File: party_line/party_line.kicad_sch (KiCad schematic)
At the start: 39 parts, among them J1 PartyLineIn, J2 PartyLineOut, J3 ExtIn, J4 Headset, SW1 SW_SPDT, SW2 SW_SPDT, U1 NE5532DR, U2 LM386G-S08-R

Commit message: layout
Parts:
- removed C8: 47u, Capacitor_SMD:C_Elec_6.3x5.4, symbol Device:C
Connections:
- net Out_L: now also R15.1; no longer R16.1
- net Out_R: now also R16.1; no longer R15.1
- net PIn_A: now also SW2.3 (C); no longer C7.1
- net PIn_B: now also SW2.1 (A)
- net at C7.2: now also C9.2, RV2.1; no longer SW2.3 (C)
- new net: C7.1, SW2.2 (B)
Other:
- moved on the sheet: C7, SW2
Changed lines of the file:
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@@
+	)
+	(junction
+		(at 175.26 45.72)
+		(diameter 0)
+		(color 0 0 0 0)
 	)
 	(junction
@@
 	)
 	(junction
-		(at 175.26 45.72)
-		(diameter 0)
-		(color 0 0 0 0)
-	)
-	(junction
 		(at 233.68 87.63)
 		(diameter 0)
@@
 	(wire
 		(pts
+			(xy 156.21 34.29) (xy 160.02 34.29)
+		)
+		(stroke
+			(width 0)
+			(type default)
+		)
+	)
+	(wire
+		(pts
 			(xy 175.26 45.72) (xy 175.26 48.26)
 		)
@@
 	(wire
 		(pts
-			(xy 177.8 35.56) (xy 177.8 22.86)
-		)
-		(stroke
-			(width 0)
-			(type default)
-		)
-	)
-	(wire
-		(pts
 			(xy 125.73 114.3) (xy 125.73 87.63)
 		)
@@
 	(wire
 		(pts
+			(xy 160.02 26.67) (xy 163.83 26.67)
+		)
+		(stroke
+			(width 0)
+			(type default)
+		)
+	)
+	(wire
+		(pts
 			(xy 123.19 39.37) (xy 123.19 45.72)
 		)
@@
 	(wire
 		(pts
-			(xy 156.21 34.29) (xy 160.02 34.29)
-		)
-		(stroke
-			(width 0)
-			(type default)
-		)
-	)
-	(wire
-		(pts
 			(xy 148.59 87.63) (xy 152.4 87.63)
 		)
@@
 	(wire
 		(pts
-			(xy 167.64 22.86) (xy 177.8 22.86)
+			(xy 181.61 45.72) (xy 175.26 45.72)
 		)
 		(stroke
@@
 	(wire
 		(pts
+			(xy 181.61 29.21) (xy 181.61 45.72)
+		)
+		(stroke
+			(width 0)
+			(type default)
+		)
+	)
+	(wire
+		(pts
 			(xy 156.21 45.72) (xy 160.02 45.72)
 		)
@@
 	(wire
 		(pts
+			(xy 160.02 22.86) (xy 160.02 26.67)
+		)
+		(stroke
+			(width 0)
+			(type default)
+		)
+	)
+	(wire
+		(pts
 			(xy 189.23 45.72) (xy 204.47 45.72)
 		)
@@
 	(wire
 		(pts
-			(xy 172.72 34.29) (xy 167.64 34.29)
-		)
-		(stroke
-			(width 0)
-			(type default)
-		)
-	)
-	(wire
-		(pts
 			(xy 107.95 114.3) (xy 107.95 96.52)
 		)
@@
 	(wire
 		(pts
+			(xy 160.02 34.29) (xy 160.02 31.75)
+		)
+		(stroke
+			(width 0)
+			(type default)
+		)
+	)
+	(wire
+		(pts
 			(xy 111.76 39.37) (xy 123.19 39.37)
 		)
@@
 		(pts
 			(xy 111.76 38.1) (xy 111.76 39.37)
+		)
+		(stroke
+			(width 0)
+			(type default)
+		)
+	)
+	(wire
+		(pts
+			(xy 160.02 31.75) (xy 163.83 31.75)
 		)
 		(stroke
@@
 	(global_label "Out_R"
 		(shape input)
-		(at 261.62 77.47 0)
+		(at 261.62 87.63 0)
 		(fields_autoplaced yes)
 		(effects
@@
 		)
 		(property "Intersheetrefs" "${INTERSHEET_REFS}"
-			(at 270.048 77.47 0)
+			(at 270.048 87.63 0)
 			(effects
 				(font
@@
 	(global_label "Out_L"
 		(shape input)
-		(at 261.62 87.63 0)
+		(at 261.62 77.47 0)
 		(fields_autoplaced yes)
 		(effects
@@
 		)
 		(property "Intersheetrefs" "${INTERSHEET_REFS}"
-			(at 269.8061 87.63 0)
+			(at 269.8061 77.47 0)
 			(effects
 				(font
@@
 	(symbol
 		(lib_id "Device:C")
-		(at 163.83 22.86 90)
+		(at 177.8 29.21 90)
 		(unit 1)
 		(exclude_from_sim no)
@@
 		(fields_autoplaced yes)
 		(property "Reference" "C7"
-			(at 162.5599 19.05 0)
+			(at 176.5299 25.4 0)
 			(effects
 				(font
@@
 		)
 		(property "Value" "47u"
-			(at 165.0999 19.05 0)
+			(at 179.0699 25.4 0)
 			(effects
 				(font
@@
 		)
 		(property "Footprint" "Capacitor_SMD:C_Elec_6.3x5.4"
-			(at 167.64 21.8948 0)
+			(at 181.61 28.2448 0)
 			(effects
 				(font
@@
 		)
 		(property "Datasheet" "~"
-			(at 163.83 22.86 0)
+			(at 177.8 29.21 0)
 			(effects
 				(font
@@
 		)
 		(property "Description" "C72522"
-			(at 163.83 22.86 0)
+			(at 177.8 29.21 0)
 			(effects
 				(font
@@
 	(symbol
 		(lib_id "Switch:SW_SPDT")
-		(at 175.26 40.64 90)
+		(at 168.91 29.21 180)
 		(unit 1)
 		(exclude_from_sim no)
@@
 		(fields_autoplaced yes)
 		(property "Reference" "SW2"
-			(at 180.34 39.3699 90)
-			(effects
-				(font
-					(size 1.27 1.27)
-				)
-				(justify right)
+			(at 168.91 20.32 0)
+			(effects
+				(font
+					(size 1.27 1.27)
+				)
 			)
 		)
 		(property "Value" "SW_SPDT"
-			(at 180.34 41.9099 90)
-			(effects
-				(font
-					(size 1.27 1.27)
-				)
-				(justify right)
+			(at 168.91 22.86 0)
+			(effects
+				(font
+					(size 1.27 1.27)
+				)
 			)
 		)
 		(property "Footprint" "Connector_PinSocket_2.54mm:PinSocket_1x03_P2.54mm_Vertical"
-			(at 175.26 40.64 0)
+			(at 168.91 29.21 0)
 			(effects
 				(font
@@
 		)
 		(property "Datasheet" "~"
-			(at 182.88 40.64 0)
+			(at 168.91 21.59 0)
 			(effects
 				(font
@@
 		)
 		(property "Description" "Switch, single pole double throw"
-			(at 175.26 40.64 0)
+			(at 168.91 29.21 0)
 			(effects
 				(font
@@
 					(unit 1)
 				)
-			)
-		)
-	)
-	(symbol
-		(lib_id "Device:C")
-		(at 163.83 34.29 90)
-		(unit 1)
-		(exclude_from_sim no)
-		(in_bom yes)
-		(on_board yes)
-		(dnp no)
-		(fields_autoplaced yes)
-		(property "Reference" "C8"
-			(at 162.5599 30.48 0)
-			(effects
-				(font
-					(size 1.27 1.27)
-				)
-				(justify left)
-			)
-		)
-		(property "Value" "47u"
-			(at 165.0999 30.48 0)
-			(effects
-				(font
-					(size 1.27 1.27)
-				)
-				(justify left)
-			)
-		)
-		(property "Footprint" "Capacitor_SMD:C_Elec_6.3x5.4"
-			(at 167.64 33.3248 0)
-			(effects
-				(font
-					(size 1.27 1.27)
-				)
-				(hide yes)
-			)
-		)
-		(property "Datasheet" "~"
-			(at 163.83 34.29 0)
-			(effects
-				(font
-					(size 1.27 1.27)
-				)
-				(hide yes)
-			)
-		)
-		(property "Description" "C72522"
-			(at 163.83 34.29 0)
-			(effects
-				(font
-					(size 1.27 1.27)
-				)
-				(hide yes)
-			)
-		)
-		(pin "2"
-		)
-		(pin "1"
-		)
-		(instances
-			(project "party_line"
-				(path "/494218c4-6a71-4a74-bdac-47238e7945be"
-					(reference "C8")
-					(unit 1)
-				)

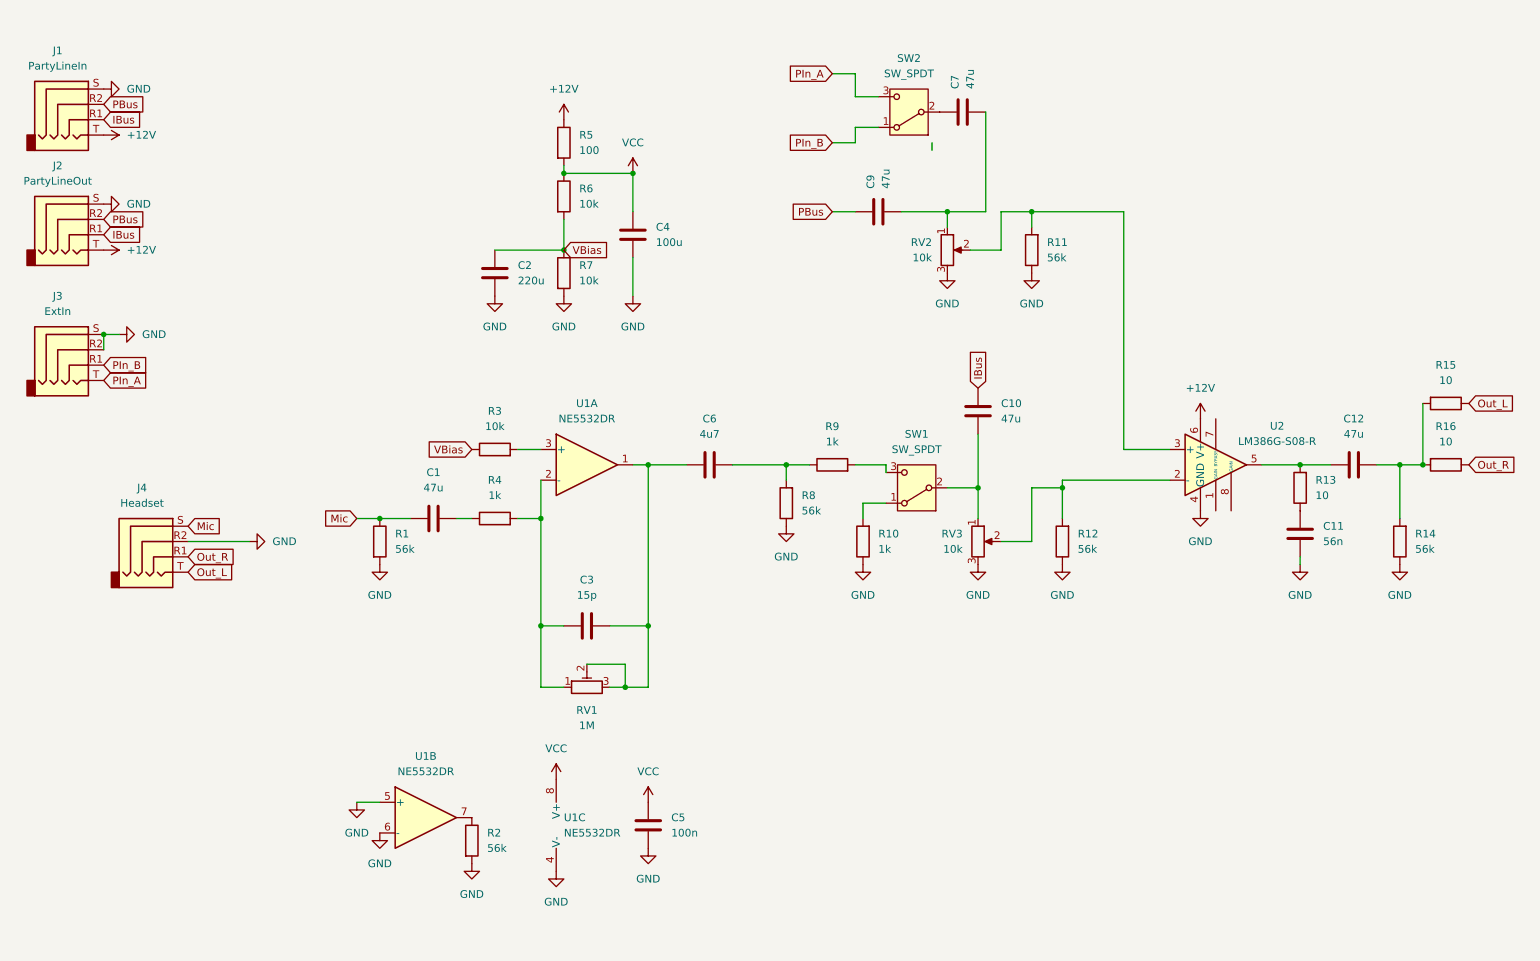
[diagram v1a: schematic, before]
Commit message: reposition jacks
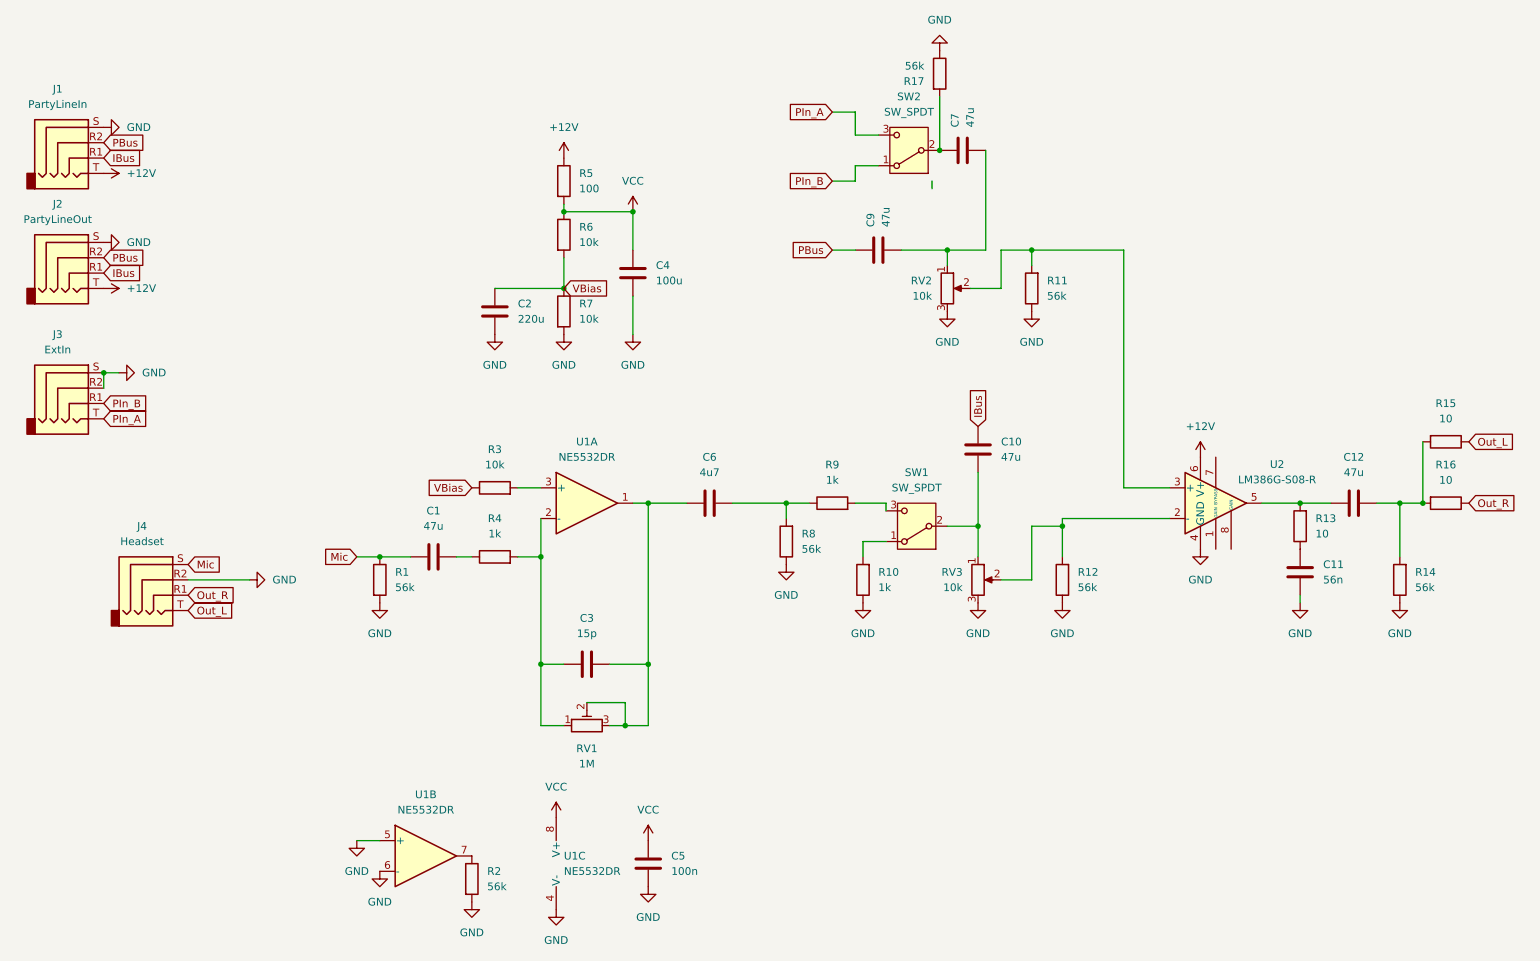
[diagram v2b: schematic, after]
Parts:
- added R17: 56k, Resistor_SMD:R_0805_2012Metric_Pad1.20x1.40mm_HandSolder, symbol Device:R
- J3: LCSC (none) -> C431535
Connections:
- net GND: now also R17.1
- net at C7.1, SW2.2 (B): now also R17.2
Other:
- moved on the sheet: C1, C10, C11, C12, C2, C3, C4, C5, C6, C7, C9, J1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
